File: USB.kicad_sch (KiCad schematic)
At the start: 0 parts

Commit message: added USB-C connector
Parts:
- added J1: USB_C_Receptacle_USB2.0_16P, Connector_USB:USB_C_Receptacle_GCT_USB4105-xx-A_16P_TopMnt_Horizontal, symbol Connector:USB_C_Receptacle_USB2.0_16P
- added R1, R2: 5.1k, symbol Device:R
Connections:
- new net +5V_USB: J1.A4 (VBUS), J1.A9 (VBUS), J1.B4 (VBUS), J1.B9 (VBUS)
- new net CC1: J1.A5 (CC1), R1.1
- new net CC2: J1.B5 (CC2), R2.1
- new net GND: J1.A1 (GND), J1.A12 (GND), J1.B1 (GND), J1.B12 (GND), J1.S1 (SHIELD), R1.2, R2.2
- new net USB_D+: J1.A6 (D+), J1.B6 (D+)
- new net USB_D-: J1.A7 (D-), J1.B7 (D-)
- no-connect marks 0 -> 2

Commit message: USB and PWR sch
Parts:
- added C1: 10u, symbol Device:C
- added D1: 1N5819HW-7-F, symbol Device:D_Schottky
- added D2, D3, D4: TODO, symbol Device:D_TVS
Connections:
- net +5V_USB: now also C1.1, D1.1 (K); no longer J1.A4 (VBUS), J1.A9 (VBUS), J1.B4 (VBUS), J1.B9 (VBUS)
- net GND: now also C1.2, D2.1 (A1), D3.1 (A1), D4.1 (A1)
- net USB_D+: now also D2.2 (A2)
- net USB_D-: now also D3.2 (A2)
- new net VBUSB: D1.2 (A), D4.2 (A2), J1.A4 (VBUS), J1.A9 (VBUS), J1.B4 (VBUS), J1.B9 (VBUS)
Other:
- title: (none) -> USB

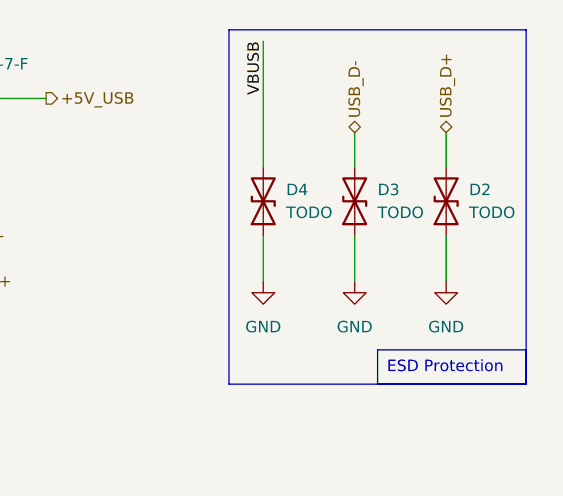
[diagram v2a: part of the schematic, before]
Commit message: add P/N
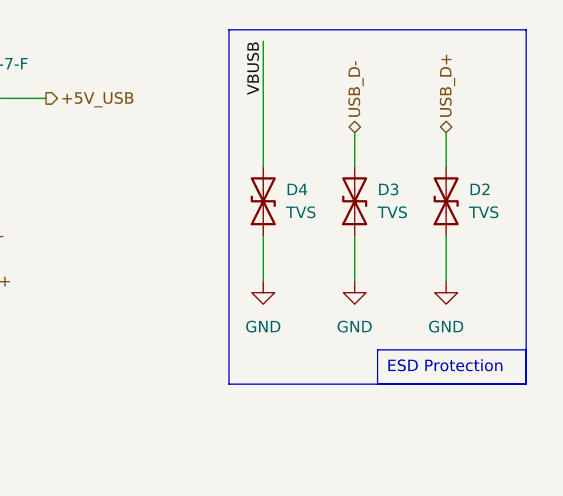
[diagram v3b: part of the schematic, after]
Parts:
- C1: P/N (none) -> MLAST168BB5106MTNA01
- D2, D3, D4: value TODO -> TVS; P/N (none) -> CPDUC5V0R-HF
- R1, R2: P/N (none) -> CRCW06035K10FKEC
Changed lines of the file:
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@@
+			)
+		)
+		(property "P/N" "CRCW06035K10FKEC"
+			(at 40.64 38.1 0)
+			(effects
+				(font
+					(size 1.27 1.27)
+				)
+				(hide yes)
 			)
 		)
@@
 			)
 		)
-		(property "Value" "TODO"
+		(property "Value" "TVS"
 			(at 140.97 40.6399 90)
 			(effects
@@
 			)
 		)
+		(property "P/N" "CPDUC5V0R-HF "
+			(at 138.43 39.37 0)
+			(effects
+				(font
+					(size 1.27 1.27)
+				)
+				(hide yes)
+			)
+		)
 		(pin "1"
 		)
@@
 			)
 		)
+		(property "P/N" "MLAST168BB5106MTNA01"
+			(at 38.1 90.17 0)
+			(effects
+				(font
+					(size 1.27 1.27)
+				)
+				(hide yes)
+			)
+		)
 		(pin "2"
 		)
@@
 			)
 		)
+		(property "P/N" "CRCW06035K10FKEC"
+			(at 31.75 38.1 0)
+			(effects
+				(font
+					(size 1.27 1.27)
+				)
+				(hide yes)
+			)
+		)
 		(pin "1"
 		)
@@
 			)
 		)
-		(property "Value" "TODO"
+		(property "Value" "TVS"
 			(at 151.13 40.6399 90)
 			(effects
@@
 			)
 		)
+		(property "P/N" "CPDUC5V0R-HF "
+			(at 148.59 39.37 0)
+			(effects
+				(font
+					(size 1.27 1.27)
+				)
+				(hide yes)
+			)
+		)
 		(pin "1"
 		)
@@
 			)
 		)
-		(property "Value" "TODO"
+		(property "Value" "TVS"
 			(at 130.81 40.6399 90)
 			(effects
@@
 			(at 128.27 39.37 0)
 			(effects
+				(font
+					(size 1.27 1.27)
+				)
+				(hide yes)
+			)
+		)
+		(property "P/N" "CPDUC5V0R-HF "
+			(at 128.27 39.37 0)
+			(effects

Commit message: assign footprints
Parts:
- C1: footprint (none) -> Capacitor_SMD:C_0603_1608Metric
- D1: footprint (none) -> Diode_SMD:D_SOD-123
- D2, D3, D4: footprint (none) -> Diode_SMD:D_0603_1608Metric
- R1, R2: footprint (none) -> Resistor_SMD:R_0603_1608Metric
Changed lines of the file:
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@@
 			)
 		)
-		(property "Footprint" ""
+		(property "Footprint" "Resistor_SMD:R_0603_1608Metric"
 			(at 38.862 38.1 90)
 			(effects
@@
 			)
 		)
-		(property "Footprint" ""
+		(property "Footprint" "Diode_SMD:D_0603_1608Metric"
 			(at 138.43 39.37 0)
 			(effects
@@
 			)
 		)
-		(property "Footprint" ""
+		(property "Footprint" "Diode_SMD:D_SOD-123"
 			(at 95.25 27.94 0)
 			(effects
@@
 			)
 		)
-		(property "Footprint" ""
+		(property "Footprint" "Capacitor_SMD:C_0603_1608Metric"
 			(at 39.0652 93.98 0)
 			(effects
@@
 			)
 		)
-		(property "Footprint" ""
+		(property "Footprint" "Resistor_SMD:R_0603_1608Metric"
 			(at 29.972 38.1 90)
 			(effects
@@
 			)
 		)
-		(property "Footprint" ""
+		(property "Footprint" "Diode_SMD:D_0603_1608Metric"
 			(at 148.59 39.37 0)
 			(effects
@@
 			)
 		)
-		(property "Footprint" ""
+		(property "Footprint" "Diode_SMD:D_0603_1608Metric"
 			(at 128.27 39.37 0)
 			(effects
